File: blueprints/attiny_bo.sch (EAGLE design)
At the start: 9 parts, among them IC1 ATTiny85, IC4 LB1973M, J1 AVR_SPI_PRG_6NS

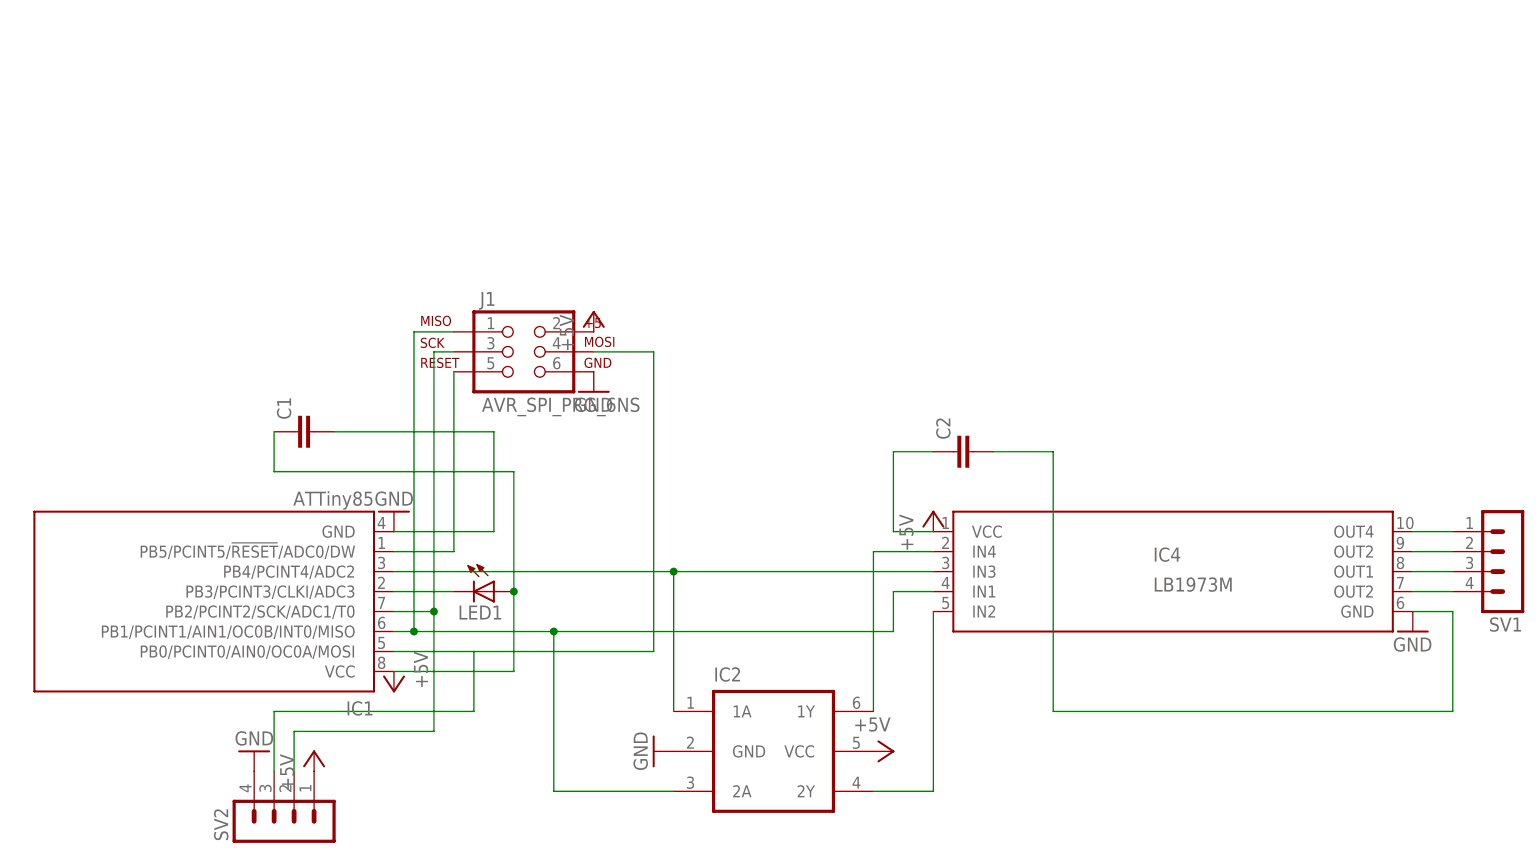
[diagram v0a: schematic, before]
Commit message: simple breakout for attiny with ISP and 2x5 breakout header with pins in port order
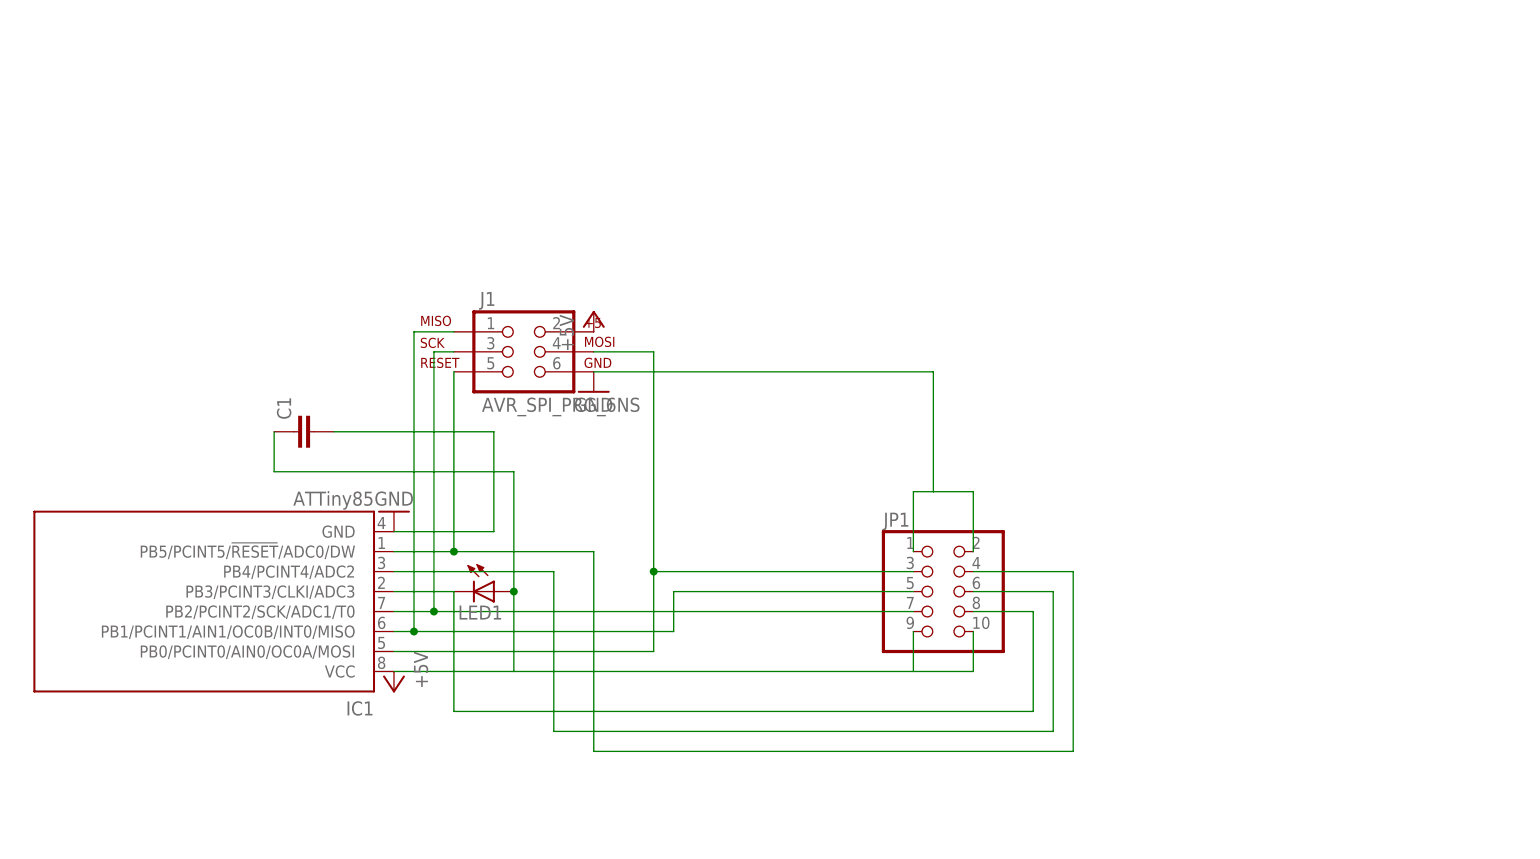
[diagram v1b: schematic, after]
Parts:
- removed C2: (no value), rcl:C-EUC0805
- removed IC2: (no value), dp_devices:IC_BUFF_SN74LVC2G17DBV
- removed IC4: LB1973M, LB1973M:LB1973M
- removed SV1, SV2: (no value), con-lstb:MA04-1
- added JP1: (no value), pinhead:PINHD-2X5
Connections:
- removed net IN2: IC2.2Y, IC4.IN2
- removed net N$2: IC2.1Y, IC4.IN4
- removed net OUT1: IC4.OUT1, SV1.3
- removed net OUT2: IC4.OUT2, SV1.4
- removed net OUT3: IC4.OUT2@1, SV1.2
- removed net OUT4: IC4.OUT4, SV1.1
- net +5V: now also JP1.10, JP1.9; no longer C2.1, IC2.VCC, IC4.VCC, SV2.1
- net GND: now also JP1.1, JP1.2; no longer C2.2, IC2.GND, IC4.GND, SV2.4
- net IN1/MISO: now also JP1.5; no longer IC2.2A, IC4.IN1
- net N$1: now also JP1.6; no longer IC2.1A, IC4.IN3
- net N$3: now also JP1.8
- net N$6: now also JP1.4
- net SCL/SCK: now also JP1.7; no longer SV2.2
- net SDA/MOSI: now also JP1.3; no longer SV2.3

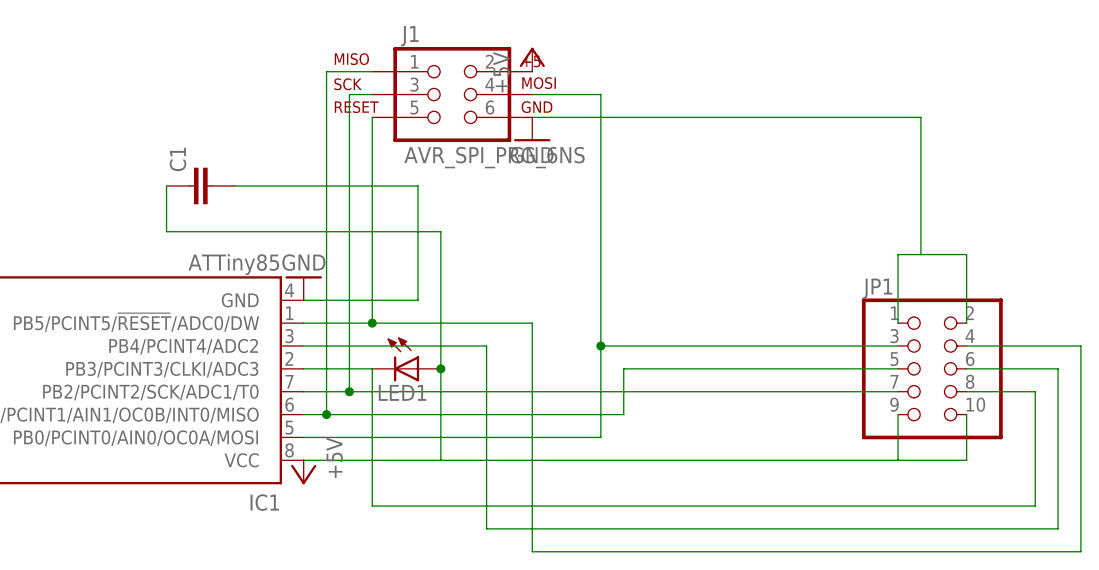
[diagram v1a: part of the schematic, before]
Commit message: put the grounds between signals in the 5x2 header
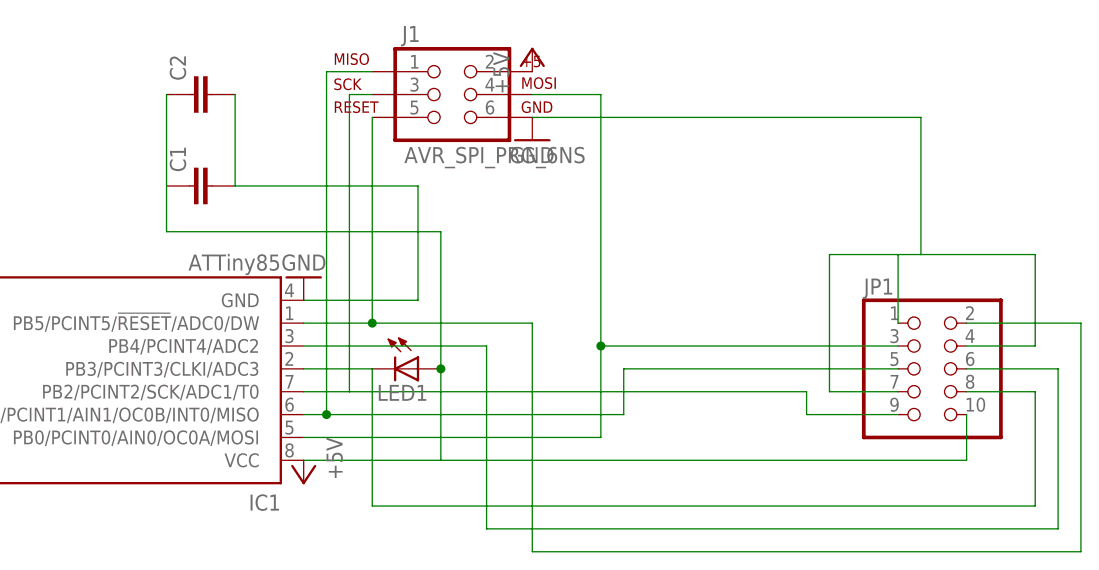
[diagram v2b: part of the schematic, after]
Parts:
- added C2: (no value), rcl:C-EUC0805
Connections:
- net +5V: now also C2.1; no longer JP1.9
- net GND: now also C2.2, JP1.4, JP1.7; no longer JP1.2
- net N$6: now also JP1.2; no longer JP1.4
- net SCL/SCK: now also JP1.9; no longer JP1.7
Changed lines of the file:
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@@
 <part name="LED1" library="SparkFun-LED" deviceset="LED" device="0603"/>
 <part name="JP1" library="pinhead" deviceset="PINHD-2X5" device=""/>
+<part name="C2" library="rcl" deviceset="C-EU" device="C0805"/>
 </parts>
 <sheets>
@@
 <instance part="LED1" gate="G$1" x="63.5" y="76.2" rot="R270"/>
 <instance part="JP1" gate="A" x="119.38" y="76.2"/>
+<instance part="C2" gate="G$1" x="38.1" y="106.68" rot="R90"/>
 </instances>
 <busses>
@@
 <wire x1="53.34" y1="71.12" x2="86.36" y2="71.12" width="0.1524" layer="91"/>
 <wire x1="86.36" y1="71.12" x2="86.36" y2="76.2" width="0.1524" layer="91"/>
+<junction x="53.34" y="71.12"/>
 <pinref part="JP1" gate="A" pin="5"/>
 <wire x1="86.36" y1="76.2" x2="116.84" y2="76.2" width="0.1524" layer="91"/>
-<junction x="53.34" y="71.12"/>
 </segment>
 </net>
@@
 <pinref part="C1" gate="G$1" pin="2"/>
 <wire x1="43.18" y1="96.52" x2="63.5" y2="96.52" width="0.1524" layer="91"/>
+<pinref part="C2" gate="G$1" pin="2"/>
+<wire x1="43.18" y1="106.68" x2="43.18" y2="96.52" width="0.1524" layer="91"/>
 </segment>
 <segment>
@@
 <pinref part="JP1" gate="A" pin="1"/>
 <wire x1="116.84" y1="81.28" x2="116.84" y2="88.9" width="0.1524" layer="91"/>
-<pinref part="JP1" gate="A" pin="2"/>
-<wire x1="124.46" y1="81.28" x2="124.46" y2="88.9" width="0.1524" layer="91"/>
-<wire x1="124.46" y1="88.9" x2="119.38" y2="88.9" width="0.1524" layer="91"/>
 <wire x1="119.38" y1="88.9" x2="116.84" y2="88.9" width="0.1524" layer="91"/>
 <wire x1="76.2" y1="104.14" x2="119.38" y2="104.14" width="0.1524" layer="91"/>
 <wire x1="119.38" y1="104.14" x2="119.38" y2="88.9" width="0.1524" layer="91"/>
+<wire x1="116.84" y1="88.9" x2="109.22" y2="88.9" width="0.1524" layer="91"/>
+<wire x1="109.22" y1="88.9" x2="109.22" y2="73.66" width="0.1524" layer="91"/>
+<pinref part="JP1" gate="A" pin="4"/>
+<wire x1="124.46" y1="78.74" x2="132.08" y2="78.74" width="0.1524" layer="91"/>
+<wire x1="132.08" y1="78.74" x2="132.08" y2="88.9" width="0.1524" layer="91"/>
+<wire x1="132.08" y1="88.9" x2="119.38" y2="88.9" width="0.1524" layer="91"/>
+<pinref part="JP1" gate="A" pin="7"/>
+<wire x1="116.84" y1="73.66" x2="109.22" y2="73.66" width="0.1524" layer="91"/>
 </segment>
 </net>
@@
 <pinref part="LED1" gate="G$1" pin="A"/>
 <junction x="66.04" y="76.2"/>
-<pinref part="JP1" gate="A" pin="9"/>
-<wire x1="116.84" y1="71.12" x2="116.84" y2="66.04" width="0.1524" layer="91"/>
 <pinref part="JP1" gate="A" pin="10"/>
-<wire x1="116.84" y1="66.04" x2="124.46" y2="66.04" width="0.1524" layer="91"/>
 <wire x1="124.46" y1="66.04" x2="124.46" y2="71.12" width="0.1524" layer="91"/>
-<wire x1="66.04" y1="66.04" x2="116.84" y2="66.04" width="0.1524" layer="91"/>
+<wire x1="66.04" y1="66.04" x2="124.46" y2="66.04" width="0.1524" layer="91"/>
+<pinref part="C2" gate="G$1" pin="1"/>
+<wire x1="35.56" y1="96.52" x2="35.56" y2="106.68" width="0.1524" layer="91"/>
 </segment>
 <segment>
@@
 <wire x1="76.2" y1="81.28" x2="76.2" y2="55.88" width="0.1524" layer="91"/>
 <wire x1="76.2" y1="55.88" x2="137.16" y2="55.88" width="0.1524" layer="91"/>
-<wire x1="137.16" y1="55.88" x2="137.16" y2="78.74" width="0.1524" layer="91"/>
-<pinref part="JP1" gate="A" pin="4"/>
-<wire x1="137.16" y1="78.74" x2="124.46" y2="78.74" width="0.1524" layer="91"/>
+<wire x1="137.16" y1="55.88" x2="137.16" y2="81.28" width="0.1524" layer="91"/>
 <junction x="58.42" y="81.28"/>
+<pinref part="JP1" gate="A" pin="2"/>
+<wire x1="124.46" y1="81.28" x2="137.16" y2="81.28" width="0.1524" layer="91"/>
 </segment>
 </net>
@@
 <pinref part="J1" gate="G$1" pin="3"/>
 <wire x1="55.88" y1="106.68" x2="58.42" y2="106.68" width="0.1524" layer="91"/>
-<pinref part="JP1" gate="A" pin="7"/>
-<wire x1="55.88" y1="73.66" x2="116.84" y2="73.66" width="0.1524" layer="91"/>
-<junction x="55.88" y="73.66"/>
+<wire x1="55.88" y1="73.66" x2="106.68" y2="73.66" width="0.1524" layer="91"/>
+<wire x1="106.68" y1="73.66" x2="106.68" y2="71.12" width="0.1524" layer="91"/>
+<pinref part="JP1" gate="A" pin="9"/>
+<wire x1="106.68" y1="71.12" x2="116.84" y2="71.12" width="0.1524" layer="91"/>
 </segment>
 </net>
@@
 <wire x1="134.62" y1="58.42" x2="134.62" y2="76.2" width="0.1524" layer="91"/>
 <pinref part="JP1" gate="A" pin="6"/>
-<wire x1="134.62" y1="76.2" x2="124.46" y2="76.2" width="0.1524" layer="91"/>
+<wire x1="124.46" y1="76.2" x2="134.62" y2="76.2" width="0.1524" layer="91"/>
 </segment>
 </net>

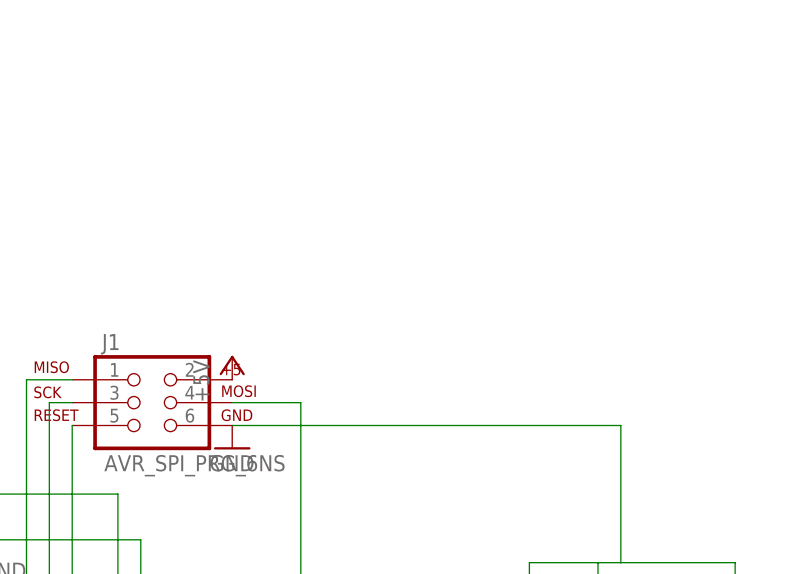
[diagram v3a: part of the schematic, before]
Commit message: mounting pads with GND access
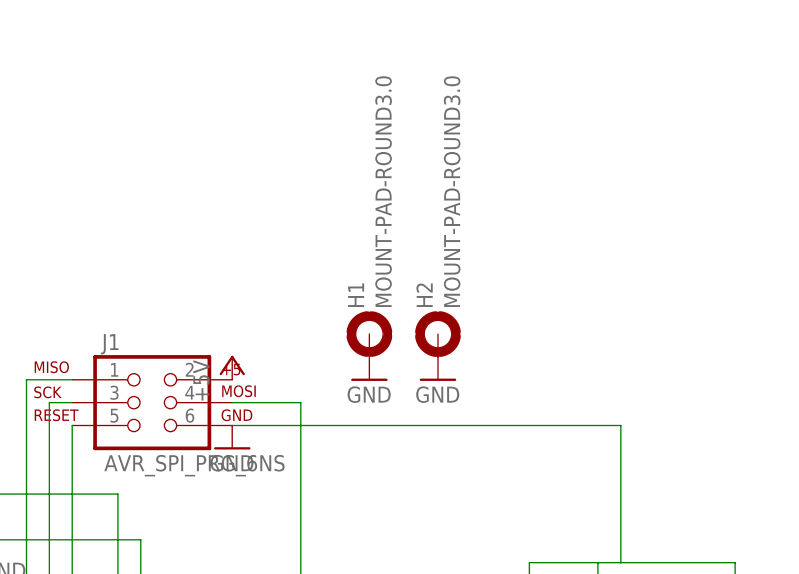
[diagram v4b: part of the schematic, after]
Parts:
- added H1, H2: MOUNT-PAD-ROUND3.0, holes:MOUNT-PAD-ROUND3.0
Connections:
- net GND: now also H1.MOUNT, H2.MOUNT
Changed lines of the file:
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@@
 <part name="JP1" library="pinhead" deviceset="PINHD-2X5" device=""/>
 <part name="C2" library="rcl" deviceset="C-EU" device="C0805"/>
+<part name="H1" library="holes" deviceset="MOUNT-PAD-ROUND" device="3.0"/>
+<part name="H2" library="holes" deviceset="MOUNT-PAD-ROUND" device="3.0"/>
+<part name="GND1" library="supply1" deviceset="GND" device=""/>
+<part name="GND2" library="supply1" deviceset="GND" device=""/>
 </parts>
 <sheets>
@@
 <instance part="JP1" gate="A" x="119.38" y="76.2"/>
 <instance part="C2" gate="G$1" x="38.1" y="106.68" rot="R90"/>
+<instance part="H1" gate="G$1" x="91.44" y="114.3" rot="R90"/>
+<instance part="H2" gate="G$1" x="99.06" y="114.3" rot="R90"/>
+<instance part="GND1" gate="1" x="99.06" y="109.22"/>
+<instance part="GND2" gate="1" x="91.44" y="109.22"/>
 </instances>
 <busses>
@@
 <wire x1="116.84" y1="73.66" x2="109.22" y2="73.66" width="0.1524" layer="91"/>
 </segment>
+<segment>
+<pinref part="H2" gate="G$1" pin="MOUNT"/>
+<pinref part="GND1" gate="1" pin="GND"/>
+</segment>
+<segment>
+<pinref part="H1" gate="G$1" pin="MOUNT"/>
+<pinref part="GND2" gate="1" pin="GND"/>
+</segment>
 </net>

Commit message: making labels
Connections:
- net IN1/MISO renamed PB1
- net N$1 renamed PB4
- net N$3 renamed PB3
- net N$6 renamed PB5
- net SCL/SCK renamed PB2
- net SDA/MOSI renamed PB0
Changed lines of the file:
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@@
 </busses>
 <nets>
-<net name="IN1/MISO" class="0">
+<net name="PB1" class="0">
 <segment>
 <pinref part="IC1" gate="G$1" pin="PB1/PCINT1/AIN1/OC0B/INT0/MISO"/>
@@
 </segment>
 </net>
-<net name="SDA/MOSI" class="0">
+<net name="PB0" class="0">
 <segment>
 <pinref part="IC1" gate="G$1" pin="PB0/PCINT0/AIN0/OC0A/MOSI"/>
@@
 </segment>
 </net>
-<net name="N$6" class="0">
+<net name="PB5" class="0">
 <segment>
 <pinref part="IC1" gate="G$1" pin="PB5/PCINT5/!RESET!/ADC0/DW"/>
@@
 </segment>
 </net>
-<net name="SCL/SCK" class="0">
+<net name="PB2" class="0">
 <segment>
 <pinref part="IC1" gate="G$1" pin="PB2/PCINT2/SCK/ADC1/T0"/>
@@
 </segment>
 </net>
-<net name="N$3" class="0">
+<net name="PB3" class="0">
 <segment>
 <pinref part="LED1" gate="G$1" pin="C"/>
@@
 </segment>
 </net>
-<net name="N$1" class="0">
+<net name="PB4" class="0">
 <segment>
 <pinref part="IC1" gate="G$1" pin="PB4/PCINT4/ADC2"/>
